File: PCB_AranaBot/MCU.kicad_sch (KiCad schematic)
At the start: 0 parts

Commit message: Update 3
Se realizó la configuración inicial del MCU, capacitores de desacople, reloj externo, y Ferrite Bread para reducir el EMI, labels con cada función de los GPIOS
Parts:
- added C1: 10u, symbol Device:C
- added C10, C9: 2.2u, symbol Device:C
- added C11, C2, C3, C4, C5, C6, C7, C8: 100n, symbol Device:C
- added C12: 1u, symbol Device:C
- added C13, C14: 10p, symbol Device:C
- added FB1: FerriteBead, symbol Device:FerriteBead
- added R1, R2, R3: 0, symbol Device:R
- added SW1: SW_DIP_x01, symbol Switch:SW_DIP_x01
- added U1: STM32F405RGTx, Package_QFP:LQFP-64_10x10mm_P0.5mm, symbol MCU_ST_STM32F4:STM32F405RGTx
- added Y1: Crystal, symbol Device:Crystal
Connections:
- new net: C14.2, R2.1, Y1.1
- new net: C13.2, R3.1, Y1.2
- new net: C11.1, C12.1, FB1.1, U1.13 (VDDA)
- new net +3V3: C1.1, C2.1, C3.1, C4.1, C5.1, C6.1, C7.1, FB1.2, R1.1, U1.1 (VBAT), U1.19 (VDD), U1.32 (VDD), U1.48 (VDD), U1.64 (VDD)
- new net ADC_TEMP: U1.17 (PA3)
- new net AN_IN: U1.10 (PC2)
- new net BOOT0: R1.2, U1.60 (BOOT0)
- new net BR_SO1: U1.27 (PB1)
- new net BR_SO2: U1.26 (PB0)
- new net CAN_RX: U1.61 (PB8)
- new net CAN_TX: U1.62 (PB9)
- new net DC_CAL: U1.33 (PB12)
- new net EN_GATE: U1.51 (PC10)
- new net FAULT: U1.53 (PC12)
- new net GND: C1.2, C10.2, C11.2, C12.2, C13.1, C14.1, C2.2, C3.2, C4.2, C5.2, C6.2, C7.2, C8.2, C9.2, SW1.1, U1.12 (VSSA), U1.18 (VSS), U1.63 (VSS)
- new net H1: U1.43 (PA10)
- new net H2: U1.42 (PA9)
- new net H3: U1.41 (PA8)
- new net HALL_1: U1.58 (PB6)
- new net HALL_2: U1.59 (PB7)
- new net HALL_3: U1.52 (PC11)
- new net L1: U1.36 (PB15)
- new net L2: U1.35 (PB14)
- new net L3: U1.34 (PB13)
- new net LED_GREEN: U1.24 (PC4)
- new net LED_RED: U1.25 (PC5)
- new net MISO_ADC_EXT2: U1.22 (PA6)
- new net NRST: C8.1, SW1.2, U1.7 (NRST)
- new net PH0: R3.2, U1.5 (PH0)
- new net PH1: R2.2, U1.6 (PH1)
- new net RX_SCL_MOSI: U1.23 (PA7), U1.29 (PB10), U1.38 (PC7)
- new net SCK_ADC_EXT: U1.21 (PA5)
- new net SENSOR1: U1.16 (PA2)
- new net SENSOR2: U1.15 (PA1)
- new net SENSOR3: U1.14 (PA0)
- new net SERVO: U1.57 (PB5)
- new net SWCLK: U1.49 (PA14)
- new net SWDIO: U1.46 (PA13)
- new net TEMP_MOTOR: U1.8 (PC0)
- new net TX_SDA_NSS: U1.20 (PA4), U1.30 (PB11), U1.37 (PC6)
- new net USB_DM: U1.44 (PA11)
- new net USB_DP: U1.45 (PA12)
- new net VCAP_1: C10.1, U1.31 (VCAP_1)
- new net VCAP_2: C9.1, U1.47 (VCAP_2)
- no-connect marks 0 -> 12
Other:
- note added: "Boot mode Tabla 7"
- note added: "Capacitores de desacople de 100n F"
- note added: "MCU"
- note added: "Reducir EMI"

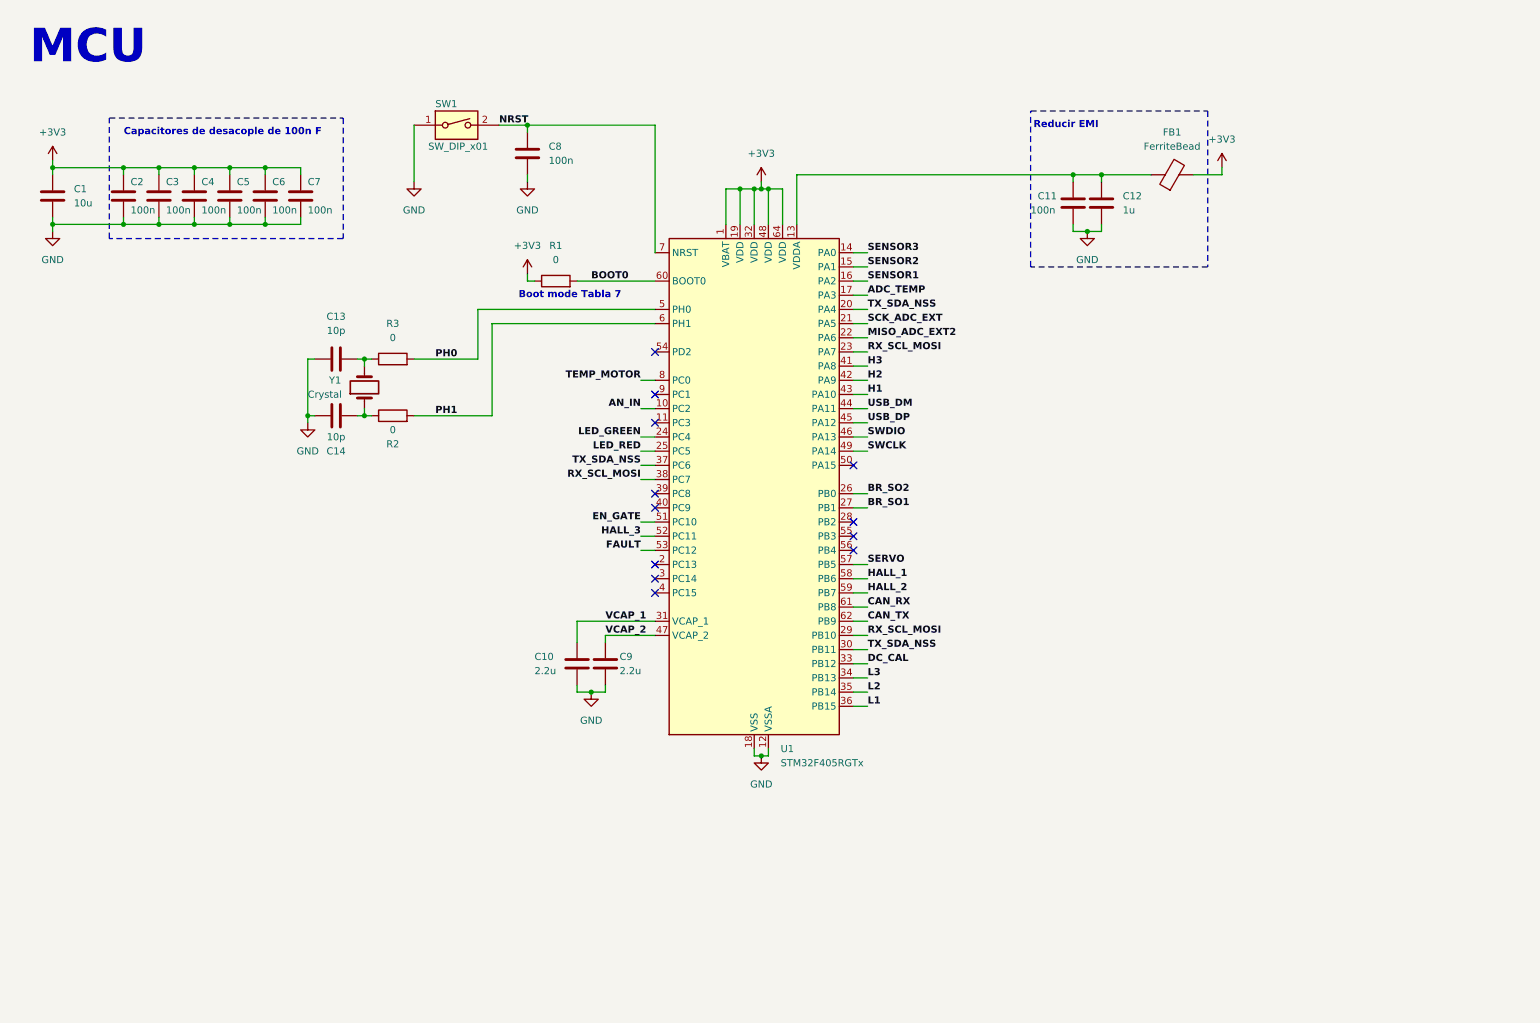
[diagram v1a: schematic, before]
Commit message: Update 4
Se finalizo las configuraciones del MCU
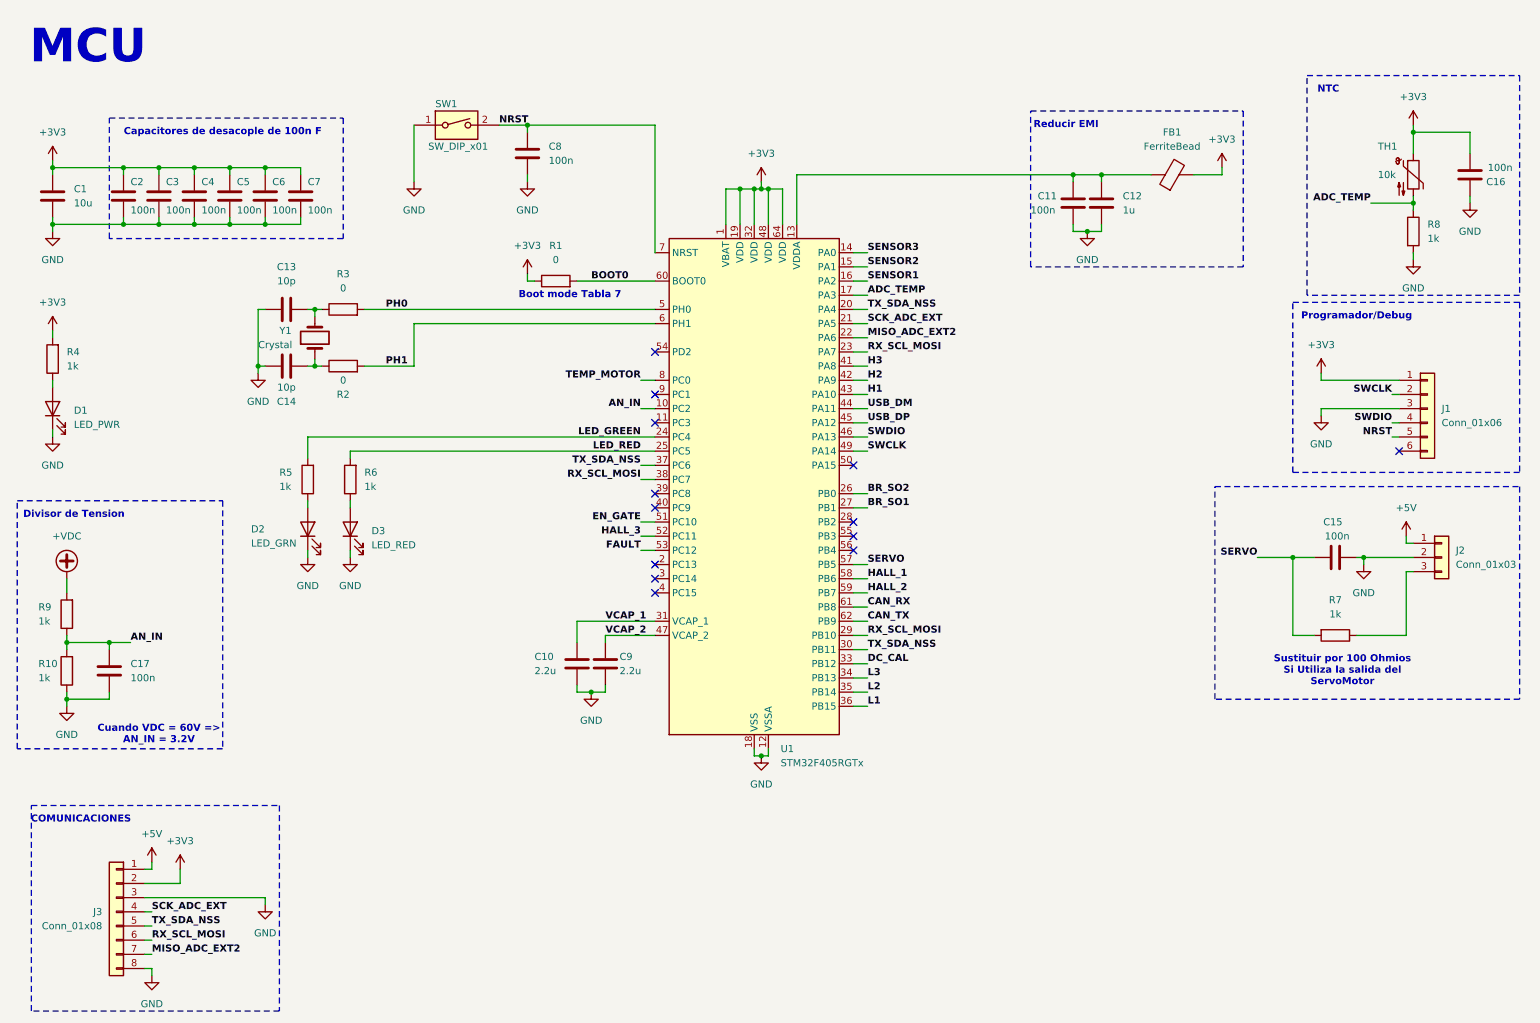
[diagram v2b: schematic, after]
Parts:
- added C15, C16, C17: 100n, symbol Device:C
- added D1: LED_PWR, symbol Device:LED
- added D2: LED_GRN, symbol Device:LED
- added D3: LED_RED, symbol Device:LED
- added J1: Conn_01x06, symbol Connector_Generic:Conn_01x06
- added J2: Conn_01x03, symbol Connector_Generic:Conn_01x03
- added J3: Conn_01x08, symbol Connector_Generic:Conn_01x08
- added R10, R4, R5, R6, R7, R8, R9: 1k, symbol Device:R
- added TH1: 10k, symbol Device:Thermistor_NTC
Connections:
- net +3V3: now also C16.2, J1.1 (Pin_1), J3.2 (Pin_2), R4.2, TH1.1
- net ADC_TEMP: now also R8.1, TH1.2
- net AN_IN: now also C17.1, R10.2, R9.1
- net GND: now also C15.2, C16.1, C17.2, D1.1 (K), D2.1 (K), D3.1 (K), J1.3 (Pin_3), J2.2 (Pin_2), J3.3 (Pin_3), J3.8 (Pin_8), R10.1, R8.2
- net LED_GREEN: now also R5.2
- net LED_RED: now also R6.2
- net MISO_ADC_EXT2: now also J3.7 (Pin_7)
- net NRST: now also J1.5 (Pin_5)
- net RX_SCL_MOSI: now also J3.6 (Pin_6)
- net SCK_ADC_EXT: now also J3.4 (Pin_4)
- net SERVO: now also C15.1, R7.2
- net SWCLK: now also J1.2 (Pin_2)
- net SWDIO: now also J1.4 (Pin_4)
- net TX_SDA_NSS: now also J3.5 (Pin_5)
- new net: J2.3 (Pin_3), R7.1
- new net: D1.2 (A), R4.1
- new net: D2.2 (A), R5.1
- new net: D3.2 (A), R6.1
- new net +5V: J2.1 (Pin_1), J3.1 (Pin_1)
- new net +VDC: R9.2
- no-connect marks 12 -> 13
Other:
- note added: "COMUNICACIONES"
- note added: "Cuando VDC = 60V => AN_IN = 3.2V"
- note added: "Divisor de Tension"
- note added: "NTC"
- note added: "Programador/Debug"
- note added: "Sustituir por 100 Ohmios Si Utiliza la salida del ServoMotor"
- moved on the sheet: C13, C14, R2, R3, Y1
